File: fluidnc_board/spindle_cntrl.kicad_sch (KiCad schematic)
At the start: 58 parts, among them J28 Screw_Terminal_01x02, J29 Screw_Terminal_01x02, J30 Screw_Terminal_01x02, Q10 IRF9Z24SPBF, Q7 BSS127S, Q8 BSS127S, Q9 ZVN4306GTA, U32 HCPL-0630, U33 HCPL-0630, U34 BD9G341EFJ, U35 LMV358, U36 LMV358, U37 OPA2182

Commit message: fixed some footprint associations, placed footprints
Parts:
- C100, C101: Digikey Part No. 1276-1048-1-ND -> (none)
- C91, C93, C94, C95, C97, C98: footprint Capacitor_SMD:C_0603_1608Metric_Pad1.05x0.95mm_HandSolder -> Capacitor_SMD:C_0603_1608Metric_Pad1.08x0.95mm_HandSolder; Digikey Part No. 1276-1941-1-ND -> (none)
- C96: Digikey Part No. 1276-1586-1-ND -> (none)
- D52, D53: Digikey Part No. 1514-BZX84C5V6TRPBFREECT-ND -> (none)
- D54: Digikey Part No. SS2150-LTPMSCT-ND -> (none)
- D55, D56: Digikey Part No. 1N4148FS-ND -> (none)
- D57: Digikey Part No. 160-1457-1-ND -> (none)
- L5: Digikey Part No. 541-2273-1-ND -> (none)
- Q10: Digikey Part No. IRF9Z24SPBF-ND -> (none)
- Q7, Q8: Digikey Part No. BSS127S-7DICT-ND -> (none)
- Q9: Digikey Part No. ZVN4306GCT-ND -> (none)
- R100, R102, R95, R96, R97, R98: Digikey Part No. 311-1.00KFRCT-ND -> (none)
- R101, R93, R94: Digikey Part No. 311-10KARCT-ND -> (none)
- R103, R106: Digikey Part No. 311-3.00KHRCT-ND -> (none)
- R104: Digikey Part No. 311-750HRCT-ND -> (none)
- R105: Digikey Part No. 311-12.0KHRCT-ND -> (none)
- R107, R108: Digikey Part No. 311-30.0KHRCT-ND -> (none)
- R109, R110: Digikey Part No. 311-24.0KHRCT-ND -> (none)
- R111: Digikey Part No. RNCF0603TKY250RCT-ND -> (none)
- R112: footprint Resistor_SMD:R_0805_2012Metric_Pad1.15x1.40mm_HandSolder -> Resistor_SMD:R_1206_3216Metric_Pad1.30x1.75mm_HandSolder; Digikey Part No. 311-.27LUCT-ND -> (none)
- R113, R114: Digikey Part No. YAG5017CT-ND -> (none)
- R115: Digikey Part No. RMCF0603FT22R0CT-ND -> (none)
- R90, R91, R92: Digikey Part No. 311-150ARCT-ND -> (none)
- R99: footprint Resistor_SMD:R_0805_2012Metric_Pad1.15x1.40mm_HandSolder -> Resistor_SMD:R_0805_2012Metric_Pad1.20x1.40mm_HandSolder; Digikey Part No. 311-47KARCT-ND -> (none)
- RN1: Digikey Part No. 505-LT5400ACMS8E-1#PBF-ND -> (none)
- U32, U33: Digikey Part No. 516-1487-1-ND -> (none)
- U34: Digikey Part No. BD9G341AEFJ-E2CT-ND -> (none)
- U35, U36: Digikey Part No. LMV358DR2GOSCT-ND -> (none)

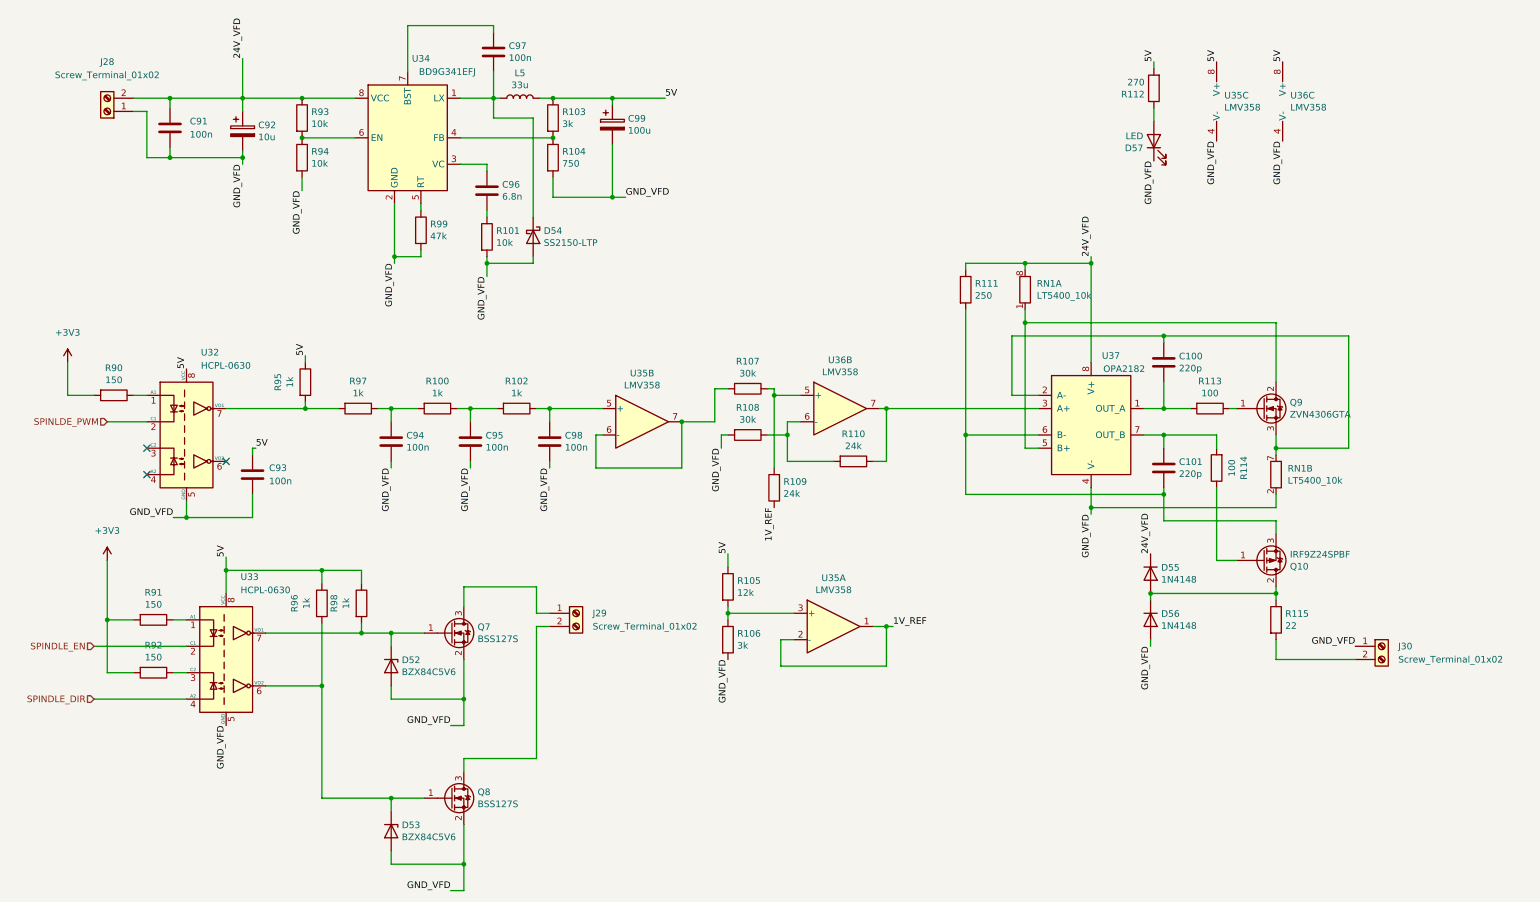
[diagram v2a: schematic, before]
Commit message: placed and routed one stepper motor unit
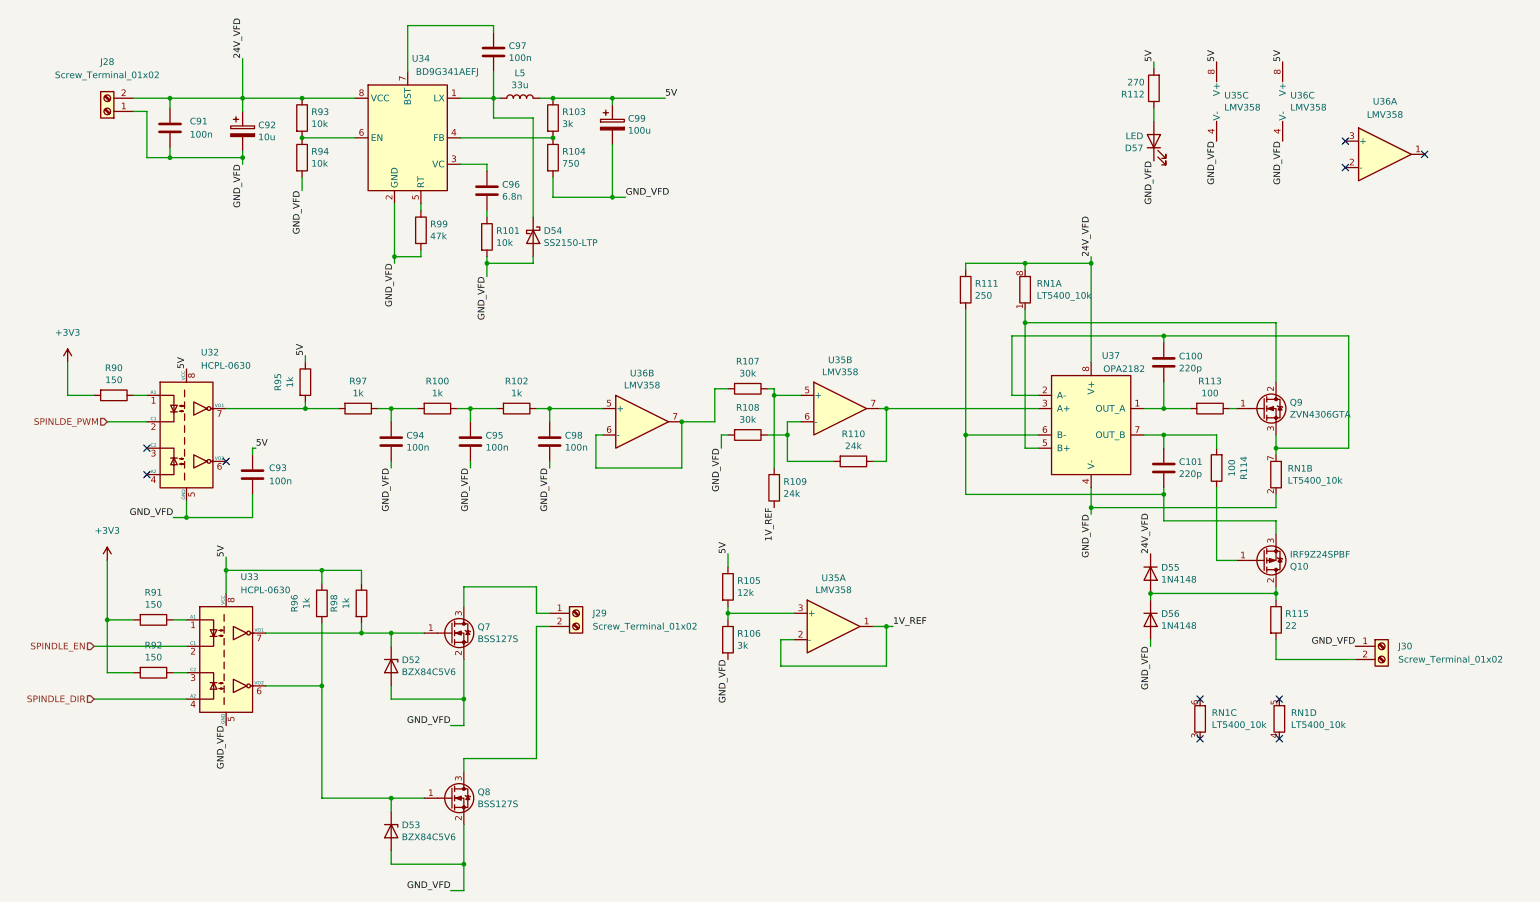
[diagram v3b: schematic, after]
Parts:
- added unit 4 of RN1
- added unit 3 of RN1
- added unit 1 of U36
- RN1: footprint Package_SO:TSSOP-8_3x3mm_P0.65mm -> Package_SO:MSOP-8-1EP_3x3mm_P0.65mm_EP1.68x1.88mm_ThermalVias
- U34: value BD9G341EFJ -> BD9G341AEFJ; symbol Regulator_Switching:BD9G341EFJ -> fluidnc_board:BD9G341AEFJ
- renumbered U36 to U35, U35 to U36
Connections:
- net GND_VFD renamed GND
- net GND: now also U34.9 (GND)
- no-connect marks 3 -> 10
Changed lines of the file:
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@@
   (junction (at 115.57 36.195) (diameter 0) (color 0 0 0 0)
   )
+  (no_connect (at 240.03 159.385))
+  (no_connect (at 240.03 151.765))
+  (no_connect (at 255.27 159.385))
+  (no_connect (at 255.27 151.765))
   (no_connect (at 52.705 106.045))
   (no_connect (at 37.465 108.585))
   (no_connect (at 37.465 103.505))
+  (no_connect (at 267.97 44.45))
+  (no_connect (at 283.21 46.99))
+  (no_connect (at 267.97 49.53))
   (wire (pts (xy 159.385 140.335) (xy 159.385 145.415))
     (stroke (width 0) (type default) (color 0 0 0 0))
@@
     (pin "1")
   )
+  (symbol (lib_id "Amplifier_Operational:LMV358") (at 275.59 46.99 0) (unit 1)
+    (in_bom yes) (on_board yes) (fields_autoplaced)
+    (property "Reference" "U36" (id 0) (at 275.59 36.83 0))
+    (property "Value" "LMV358" (id 1) (at 275.59 39.37 0))
+    (property "Footprint" "" (id 2) (at 275.59 46.99 0)
+      (effects (font (size 1.27 1.27)) hide)
+    )
+    (property "Datasheet" "http://www.ti.com/lit/ds/symlink/lmv324.pdf" (id 3) (at 275.59 46.99 0)
+      (effects (font (size 1.27 1.27)) hide)
+    )
+    (pin "1")
+    (pin "2")
+    (pin "3")
+  )
   (symbol (lib_id "Connector:Screw_Terminal_01x02") (at 120.015 135.255 0) (unit 1)
     (in_bom yes) (on_board yes) (fields_autoplaced)
@@
   (symbol (lib_id "Amplifier_Operational:LMV358") (at 132.715 98.425 0) (unit 2)
     (in_bom yes) (on_board yes)
-    (property "Reference" "U35" (id 0) (at 132.715 89.1032 0))
+    (property "Reference" "U36" (id 0) (at 132.715 89.1032 0))
     (property "Value" "LMV358" (id 1) (at 132.715 91.4146 0))
     (property "Footprint" "Package_SO:SOIC-8_3.9x4.9mm_P1.27mm" (id 2) (at 132.715 98.425 0)
@@
   (symbol (lib_id "Amplifier_Operational:LMV358") (at 170.815 95.885 0) (unit 2)
     (in_bom yes) (on_board yes)
-    (property "Reference" "U36" (id 0) (at 170.815 86.5632 0))
+    (property "Reference" "U35" (id 0) (at 170.815 86.5632 0))
     (property "Value" "LMV358" (id 1) (at 170.815 88.8746 0))
     (property "Footprint" "Package_SO:SOIC-8_3.9x4.9mm_P1.27mm" (id 2) (at 170.815 95.885 0)
@@
       (effects (font (size 1.27 1.27)) (justify left))
     )
-    (property "Footprint" "Package_SO:TSSOP-8_3x3mm_P0.65mm" (id 2) (at 204.343 73.025 90)
+    (property "Footprint" "Package_SO:MSOP-8-1EP_3x3mm_P0.65mm_EP1.68x1.88mm_ThermalVias" (id 2) (at 204.343 73.025 90)
       (effects (font (size 1.27 1.27)) hide)
     )
@@
     (pin "2")
   )
-  (symbol (lib_id "Regulator_Switching:BD9G341EFJ") (at 87.63 43.815 0) (unit 1)
+  (symbol (lib_id "fluidnc_board:BD9G341AEFJ") (at 87.63 43.815 0) (unit 1)
     (in_bom yes) (on_board yes)
     (property "Reference" "U34" (id 0) (at 90.17 28.575 0))
-    (property "Value" "BD9G341EFJ" (id 1) (at 95.25 31.115 0))
+    (property "Value" "BD9G341AEFJ" (id 1) (at 95.25 31.115 0))
     (property "Footprint" "Package_SO:HTSOP-8-1EP_3.9x4.9mm_P1.27mm_EP2.4x3.2mm_ThermalVias" (id 2) (at 90.17 55.245 0)
       (effects (font (size 1.27 1.27)) (justify left) hide)
@@
       (effects (font (size 1.27 1.27)) hide)
     )
+    (pin "9")
     (pin "1")
     (pin "2")
@@
     (pin "2")
   )
+  (symbol (lib_id "Device:R_Pack04_Split") (at 255.27 155.575 0) (unit 4)
+    (in_bom yes) (on_board yes)
+    (property "Reference" "RN1" (id 0) (at 257.5052 154.4066 0)
+      (effects (font (size 1.27 1.27)) (justify left))
+    )
+    (property "Value" "LT5400_10k" (id 1) (at 257.5052 156.718 0)
+      (effects (font (size 1.27 1.27)) (justify left))
+    )
+    (property "Footprint" "Package_SO:MSOP-8-1EP_3x3mm_P0.65mm_EP1.68x1.88mm_ThermalVias" (id 2) (at 253.238 155.575 90)
+      (effects (font (size 1.27 1.27)) hide)
+    )
+    (property "Datasheet" "~" (id 3) (at 255.27 155.575 0)
+      (effects (font (size 1.27 1.27)) hide)
+    )
+    (pin "4")
+    (pin "5")
+  )
   (symbol (lib_id "Device:C") (at 99.695 102.235 0) (unit 1)
     (in_bom yes) (on_board yes)
@@
     (pin "8")
   )
+  (symbol (lib_id "Device:R_Pack04_Split") (at 240.03 155.575 0) (unit 3)
+    (in_bom yes) (on_board yes)
+    (property "Reference" "RN1" (id 0) (at 242.2652 154.4066 0)
+      (effects (font (size 1.27 1.27)) (justify left))
+    )
+    (property "Value" "LT5400_10k" (id 1) (at 242.2652 156.718 0)
+      (effects (font (size 1.27 1.27)) (justify left))
+    )
+    (property "Footprint" "Package_SO:MSOP-8-1EP_3x3mm_P0.65mm_EP1.68x1.88mm_ThermalVias" (id 2) (at 237.998 155.575 90)
+      (effects (font (size 1.27 1.27)) hide)
+    )
+    (property "Datasheet" "~" (id 3) (at 240.03 155.575 0)
+      (effects (font (size 1.27 1.27)) hide)
+    )
+    (pin "3")
+    (pin "6")
+  )
   (symbol (lib_id "Device:R_Pack04_Split") (at 254.635 108.585 0) (unit 2)
     (in_bom yes) (on_board yes)
@@
       (effects (font (size 1.27 1.27)) (justify left))
     )
-    (property "Footprint" "Package_SO:TSSOP-8_3x3mm_P0.65mm" (id 2) (at 252.603 108.585 90)
-      (effects (font (size 1.27 1.27)) hide)
-    )
+    (property "Footprint" "Package_SO:MSOP-8-1EP_3x3mm_P0.65mm_EP1.68x1.88mm_ThermalVias" (id 2) (at 252.603 108.585 90)
+      (effects (font (size 1.27 1.27)) hide)
+    )

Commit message: one driver unit layout
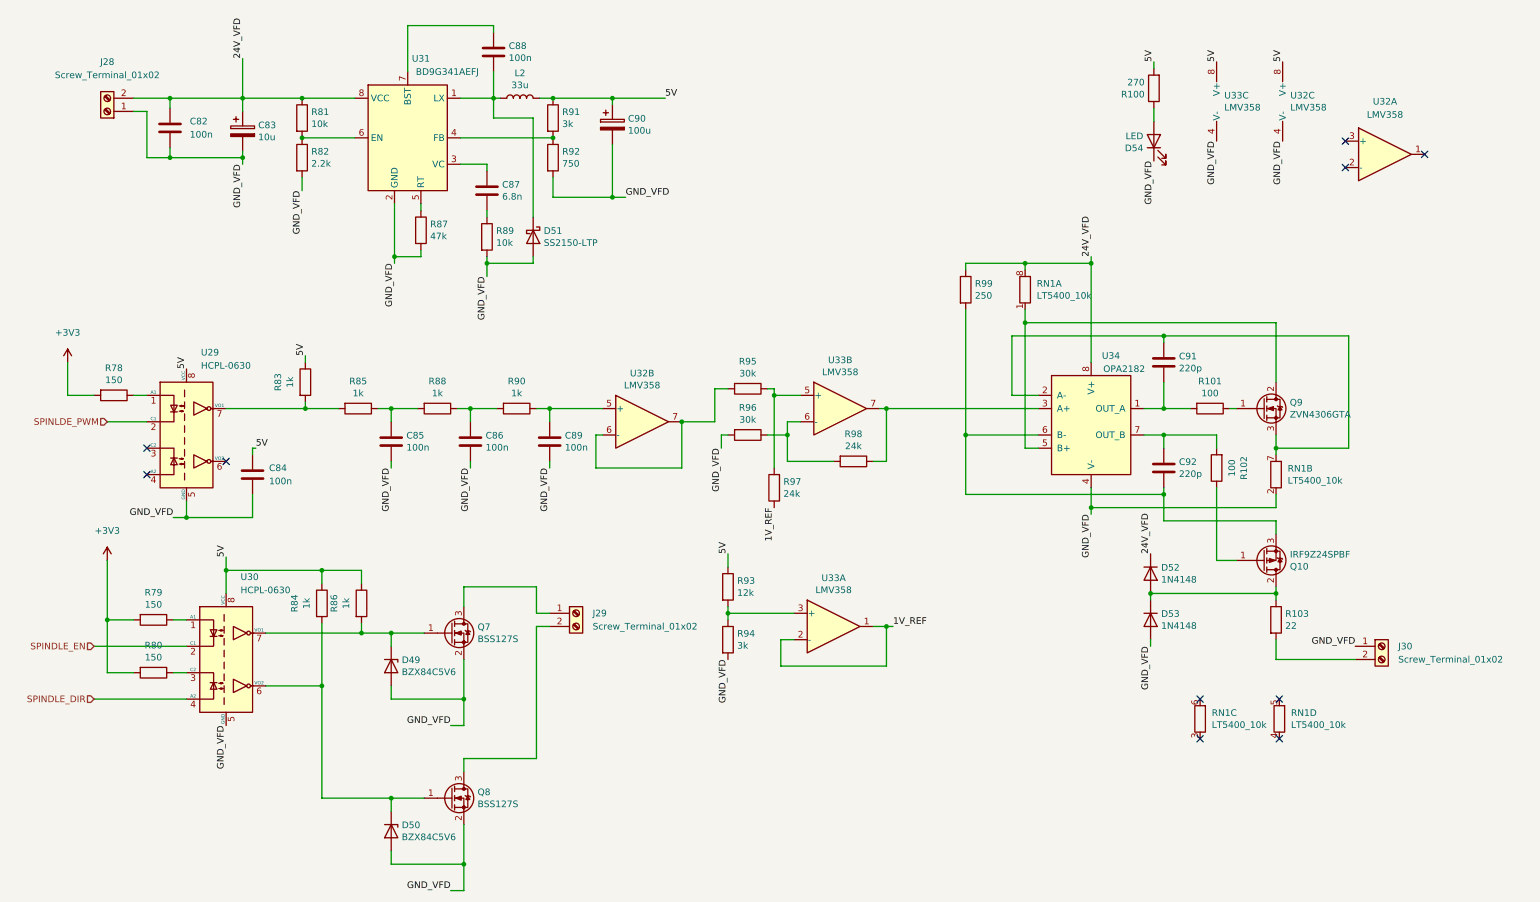
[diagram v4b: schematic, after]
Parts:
- removed R94: 10k, Resistor_SMD:R_0805_2012Metric_Pad1.20x1.40mm_HandSolder, symbol Device:R
- added R82: 2.2k, Resistor_SMD:R_0603_1608Metric_Pad0.98x0.95mm_HandSolder, symbol Device:R
- U32: renamed from U36; footprint (none) -> Package_SO:SOIC-8_3.9x4.9mm_P1.27mm
- renumbered C91 to C82, C92 to C83, C93 to C84, C94 to C85, C95 to C86, C96 to C87, C97 to C88, C98 to C89, C99 to C90, C100 to C91, C101 to C92, D52 to D49, D53 to D50, D54 to D51, D55 to D52, D56 to D53, D57 to D54, L5 to L2, R112 to R100, R113 to R101, R114 to R102, R115 to R103, R90 to R78, R91 to R79, R92 to R80, R93 to R81, R95 to R83, R96 to R84, R97 to R85, R98 to R86, R99 to R87, R100 to R88, R101 to R89, R102 to R90, R103 to R91, R104 to R92, R105 to R93, R106 to R94, R107 to R95, R108 to R96, R109 to R97, R110 to R98, R111 to R99, U32 to U29, U33 to U30, U34 to U31, U36 to U32, U35 to U33, U37 to U34
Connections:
- net GND: now also R82.2
- net at R81.2, U31.6 (EN): now also R82.1
